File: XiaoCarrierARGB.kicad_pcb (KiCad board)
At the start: 4 copper layers, 63.5 x 38.1 mm, 49 parts, among them J1 V_{IN}^{10-24V}, J2 Conn_01x08, J3 Conn_01x01, J4 Conn_01x08, J5 Conn_01x01, J6 Conn_01x06, U1 TLV75733PDBV, U2 TPP362083-T6TR, U3 XIAO-ESP32-C6-DIP, U4 74LVC1T45W6-7, U5 74LVC1T45W6-7, U6 74LVC1T45W6-7

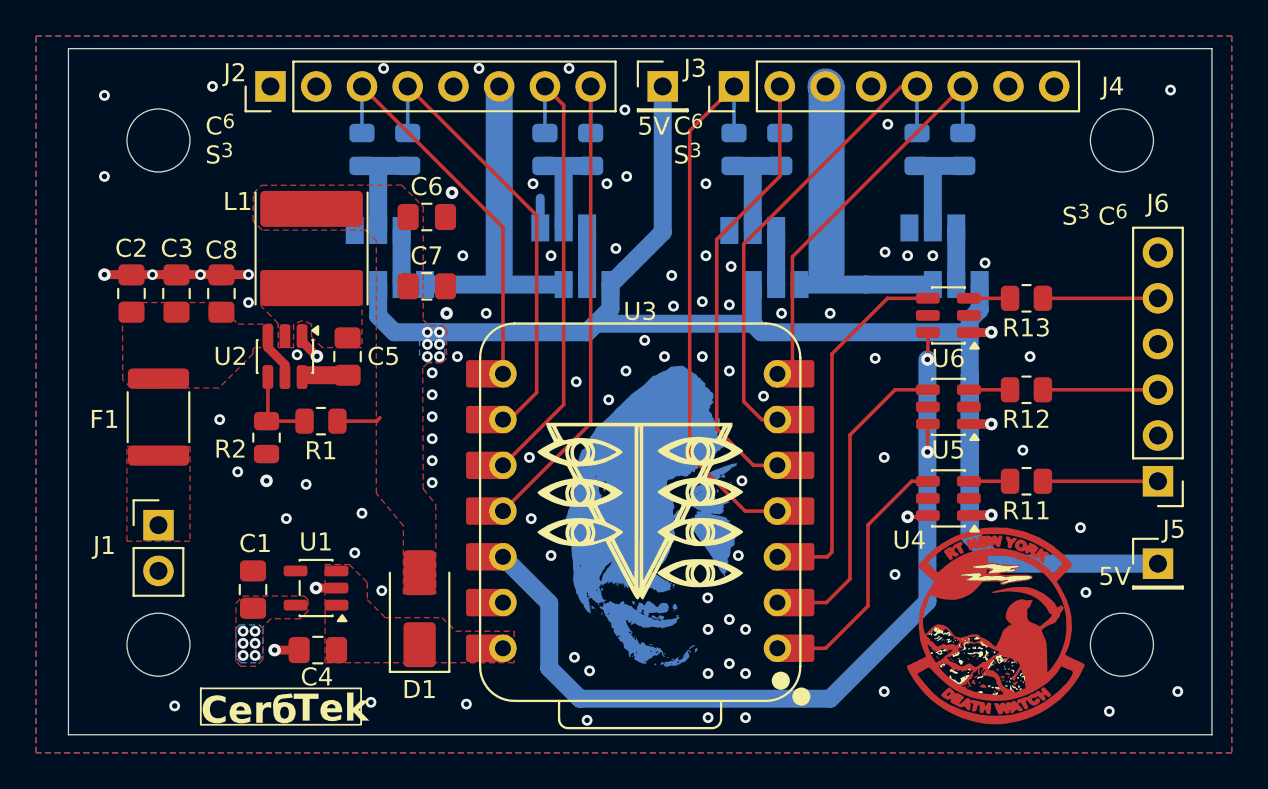
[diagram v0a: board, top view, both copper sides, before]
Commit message: added +- inidcators to Vin changed optional passives footprints to more hand solder friendly footprints
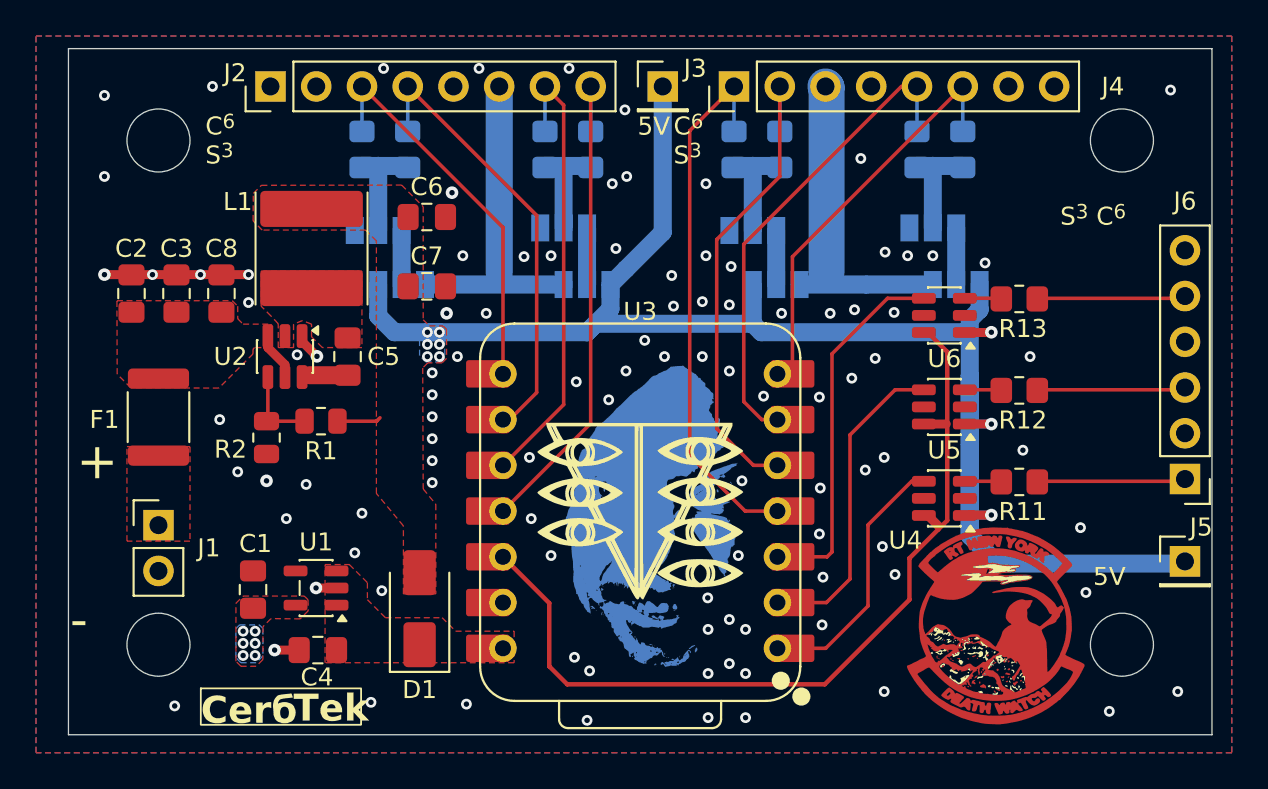
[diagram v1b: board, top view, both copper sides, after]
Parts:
- R10, R11, R12, R13, R3, R4, R5, R6, R7, R8, R9: footprint Resistor_SMD:R_0805_2012Metric -> Resistor_SMD:R_0805_2012Metric_Pad1.20x1.40mm_HandSolder
- moved J5 1.51 mm to (150.2, 109.4)
- moved J6 1.51 mm to (150.2, 104.8)
- moved R11 0.40 mm to (141.1, 105.0)
- moved R12 0.40 mm to (141.1, 99.9)
- moved R13 0.40 mm to (141.1, 94.8)
- moved U4 0.23 mm to (136.9, 105.9)
- moved U5 0.23 mm to (136.9, 100.8)
- moved U6 0.23 mm to (136.9, 95.8)
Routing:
- net +5V: track 97.5 -> 99.5 mm
- net Net-(J6-Pin_3): track 6.39 -> 8.27 mm
- net Net-(J6-Pin_1): track 6.39 -> 8.27 mm
- net Net-(J6-Pin_5): track 6.39 -> 8.27 mm
- net GND: track 13.3 -> 11.7 mm, vias 93 -> 103
- net /Xiao3v3: track 49.9 -> 48.4 mm, vias 3 -> 0
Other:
- board text added: "+"
- board text added: "-"

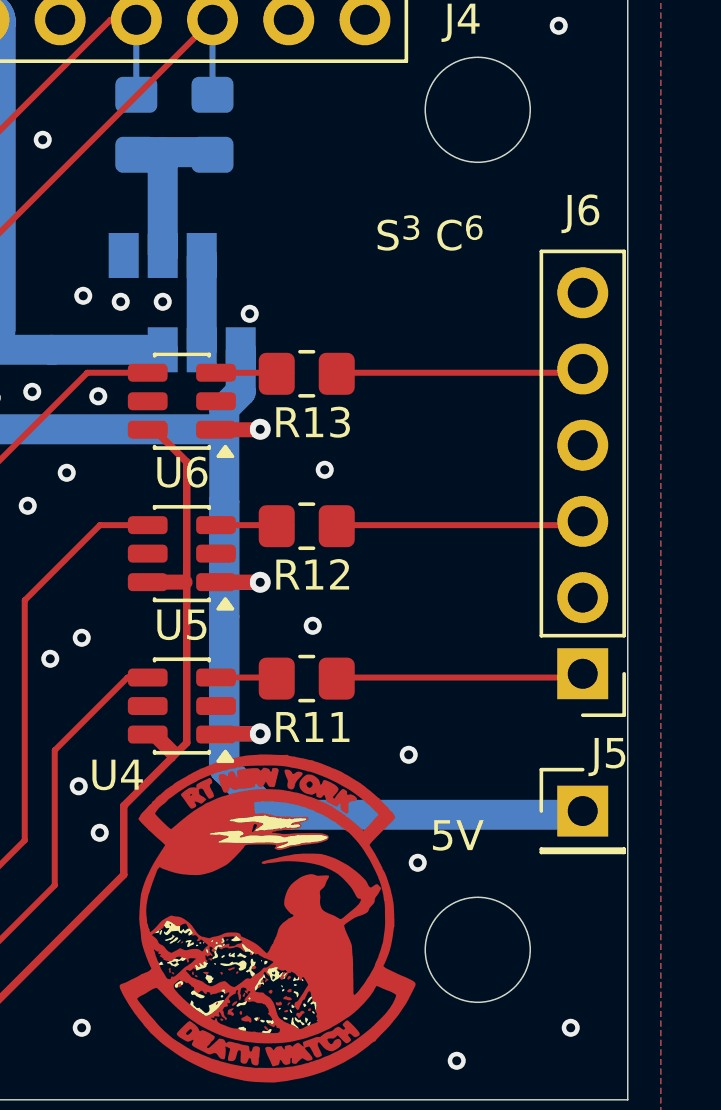
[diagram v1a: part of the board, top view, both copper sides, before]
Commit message: moved some stuff ensure screw terminal compatibility w at least VIN and Data line connections
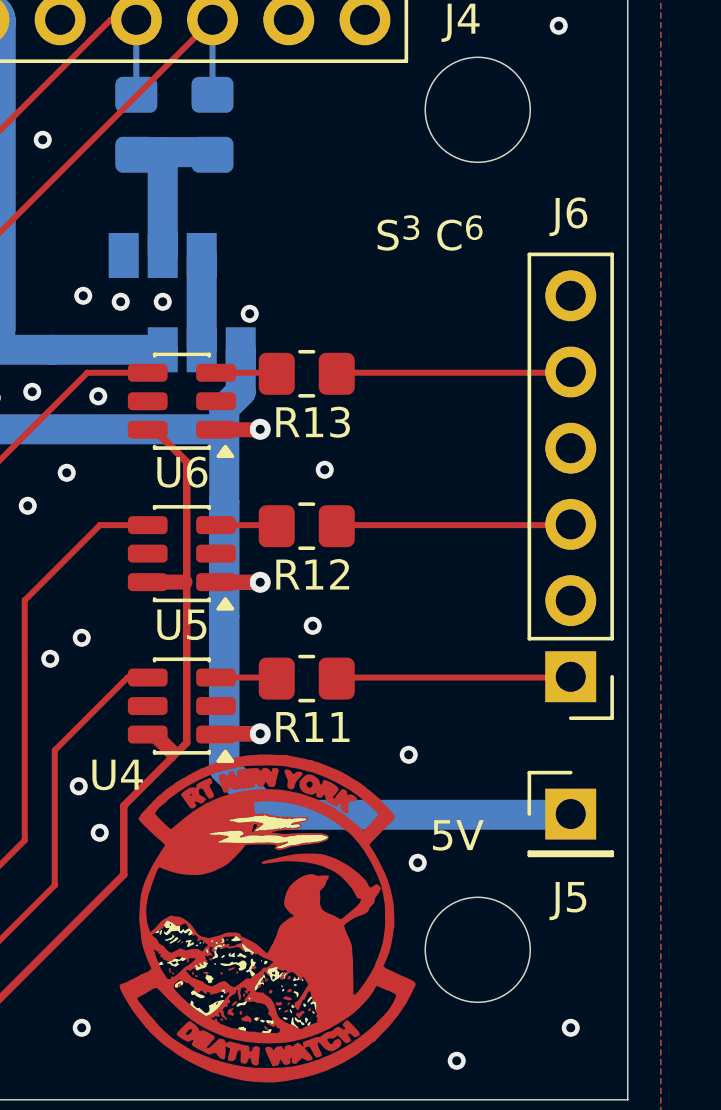
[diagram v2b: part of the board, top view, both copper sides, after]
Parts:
- moved J5 0.41 mm to (149.8, 109.5)
- moved J6 0.41 mm to (149.8, 105.0)
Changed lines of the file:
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@@
 	(footprint "Connector_PinHeader_2.54mm:PinHeader_1x01_P2.54mm_Vertical"
 		(layer "F.Cu")
-		(at 150.25 109.425)
+		(at 149.85 109.525)
 		(descr "Through hole straight pin header, 1x01, 2.54mm pitch, single row")
 		(tags "Through hole pin header THT 1x01 2.54mm single row")
 		(property "Reference" "J5"
-			(at 0.9 -1.9 0)
+			(at 0 2.8 0)
 			(layer "F.SilkS")
 			(effects
@@
 	(footprint "Connector_PinHeader_2.54mm:PinHeader_1x06_P2.54mm_Vertical"
 		(layer "F.Cu")
-		(at 150.25 104.85 180)
+		(at 149.85 104.95 180)
 		(descr "Through hole straight pin header, 1x06, 2.54mm pitch, single row")
 		(tags "Through hole pin header THT 1x06 2.54mm single row")
@@
 						(thickness 0.15)
 					)
+					(justify right)
 				)
 			)
@@
 						(thickness 0.15)
 					)
+					(justify right)
 				)
 			)
@@
 						(thickness 0.15)
 					)
+					(justify right)
 				)
 			)
@@
 	)
 	(segment
+		(start 139.85 109.55)
+		(end 138.3 108)
+		(width 1)
+		(layer "B.Cu")
+		(net "+5V")
+	)
+	(segment
 		(start 118.35 94.05)
 		(end 118.35 95.4)
@@
 	)
 	(segment
-		(start 138.3 108)
-		(end 138.3 99.1)
-		(width 1)
-		(layer "B.Cu")
-		(net "+5V")
-	)
-	(segment
 		(start 139.5 101.8)
 		(end 138.5 101.8)
@@
 	)
 	(segment
+		(start 149.825 109.55)
+		(end 139.85 109.55)
+		(width 1)
+		(layer "B.Cu")
+		(net "+5V")
+	)
+	(segment
 		(start 118.35 94.05)
 		(end 119.2 93.2)
@@
 	)
 	(segment
-		(start 139.85 109.55)
-		(end 138.3 108)
-		(width 1)
-		(layer "B.Cu")
-		(net "+5V")
-	)
-	(segment
 		(start 138.3 102)
 		(end 138.3 102.95)
@@
 	)
 	(segment
-		(start 150.25 109.425)
-		(end 150.125 109.55)
+		(start 105.45 95.8)
+		(end 106.35 96.7)
 		(width 1)
 		(layer "B.Cu")
@@
 	)
 	(segment
-		(start 105.45 95.8)
-		(end 106.35 96.7)
+		(start 138.3 99.1)
+		(end 138.3 96.7)
 		(width 1)
 		(layer "B.Cu")
@@
 	)
 	(segment
-		(start 138.3 99.1)
-		(end 138.3 96.7)
+		(start 149.85 109.525)
+		(end 149.825 109.55)
 		(width 1)
 		(layer "B.Cu")
@@
 	)
 	(segment
-		(start 138.3 96)
-		(end 138.85 95.45)
+		(start 138.3 108)
+		(end 138.3 99.1)
 		(width 1)
 		(layer "B.Cu")
@@
 	)
 	(segment
-		(start 118.35 95.4)
-		(end 117.05 96.7)
+		(start 138.3 96)
+		(end 138.85 95.45)
 		(width 1)
 		(layer "B.Cu")
@@
 	)
 	(segment
-		(start 150.125 109.55)
-		(end 139.85 109.55)
+		(start 118.35 95.4)
+		(end 117.05 96.7)
 		(width 1)
 		(layer "B.Cu")
@@
 	)
 	(segment
-		(start 142.085 99.895)
-		(end 150.125 99.895)
+		(start 149.825 99.895)
+		(end 149.85 99.87)
 		(width 0.2)
 		(layer "F.Cu")
@@
 	)
 	(segment
-		(start 150.125 99.895)
-		(end 150.25 99.77)
+		(start 142.085 99.895)
+		(end 149.825 99.895)
 		(width 0.2)
 		(layer "F.Cu")
@@
 	)
 	(segment
-		(start 142.085 94.815)
-		(end 150.125 94.815)
+		(start 142.05 94.85)
+		(end 142.085 94.815)
 		(width 0.2)
 		(layer "F.Cu")
@@
 	)
 	(segment
-		(start 150.125 94.815)
-		(end 150.25 94.69)
+		(start 142.085 94.815)
+		(end 149.825 94.815)
 		(width 0.2)
 		(layer "F.Cu")
@@
 	)
 	(segment
-		(start 142.05 94.85)
-		(end 142.085 94.815)
+		(start 149.825 94.815)
+		(end 149.85 94.79)
 		(width 0.2)
 		(layer "F.Cu")
@@
 	)
 	(segment
-		(start 142.085 104.975)
-		(end 150.125 104.975)
+		(start 149.825 104.975)
+		(end 149.85 104.95)
 		(width 0.2)
 		(layer "F.Cu")
@@
 	)
 	(segment
-		(start 150.125 104.975)
-		(end 150.25 104.85)
+		(start 142.085 104.975)
+		(end 149.825 104.975)
 		(width 0.2)
 		(layer "F.Cu")

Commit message: added some silk screen
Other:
- board text added: "12-24V only"
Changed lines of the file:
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@@
+		)
+	)
+	(gr_text "12-24V only"
+		(at 98.25 106.05 0)
+		(layer "B.SilkS" knockout)
+		(effects
+			(font
+				(size 1 1)
+				(thickness 0.15)
+			)
+			(justify left bottom mirror)
 		)
 	)
@@
 			)
 			(justify bottom mirror)
+		)
+	)
+	(gr_text "-"
+		(at 98.363095 111.55 -0)
+		(layer "B.SilkS")
+		(effects
+			(font
+				(size 2 2)
+			)
+			(justify left bottom mirror)
+		)
+	)
+	(gr_text "+"
+		(at 97.05 108.55 -0)
+		(layer "B.SilkS" knockout)
+		(effects
+			(font
+				(size 2 2)
+			)
+			(justify bottom mirror)

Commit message: Finalized Design export gerbers for manufacturing
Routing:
- net GND: vias 103 -> 104
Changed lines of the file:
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@@
+	)
+	(via
+		(at 140.05 97.65)
+		(size 0.6)
+		(drill 0.3)
+		(layers "F.Cu" "B.Cu")
+		(free yes)
+		(net "GND")
 	)
 	(via
@@
 	)
 	(via
-		(at 108.45 105.05)
+		(at 109.05 105.25)
 		(size 0.6)
 		(drill 0.3)
@@
 	)
 	(via
-		(at 108.45 100.17)
+		(at 109.05 100.37)
 		(size 0.6)
 		(drill 0.3)
@@
 	)
 	(via
-		(at 108.45 103.83)
+		(at 109.05 104.03)
 		(size 0.6)
 		(drill 0.3)
@@
 	)
 	(via
-		(at 108.45 101.39)
+		(at 109.05 101.59)
 		(size 0.6)
 		(drill 0.3)
@@
 	)
 	(via
-		(at 108.45 98.95)
+		(at 109.05 99.15)
 		(size 0.6)
 		(drill 0.3)
@@
 	)
 	(via
-		(at 108.45 102.61)
-		(size 0.6)
-		(drill 0.3)
+		(at 109.05 102.81)
+		(size 0.6)
+		(drill 0.3)
